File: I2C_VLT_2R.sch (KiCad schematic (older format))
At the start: 5 parts, among them Q14 BSS138, Q15 BSS138

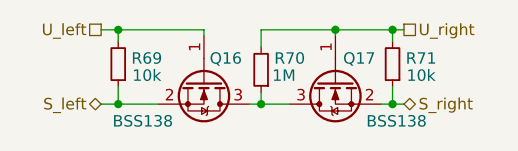
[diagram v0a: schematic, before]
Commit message: Завершена трассировка печатной платы. Исправлены ошибки в схема.
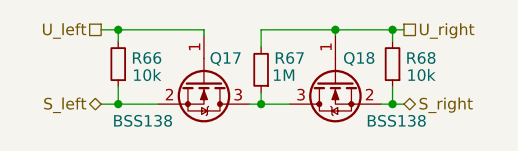
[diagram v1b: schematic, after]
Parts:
- renumbered Q14 to Q17, Q15 to Q18
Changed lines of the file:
@@
 AR Path="/63EB474D/6022B564" Ref="Q?"  Part="1"
 AR Path="/64080380/6022B564" Ref="Q?"  Part="1"
-AR Path="/61C817F1/61DF5D35/6022B564" Ref="Q14"  Part="1"
-AR Path="/61C817F1/61DF5D57/6022B564" Ref="Q16"  Part="1"
+AR Path="/61C817F1/61DF5D35/6022B564" Ref="Q17"  Part="1"
+AR Path="/61C817F1/61DF5D57/6022B564" Ref="Q19"  Part="1"
 AR Path="/63E242A3/61DF5D35/6022B564" Ref="Q?"  Part="1"
 AR Path="/63E242A3/61DF5D57/6022B564" Ref="Q?"  Part="1"
-F 0 "Q16" V 5225 1800 50  0000 L CNN
+F 0 "Q17" V 5225 1800 50  0000 L CNN
 F 1 "BSS138" V 5500 1375 50  0000 L CNN
 F 2 "Package_TO_SOT_SMD:SOT-23" H 5525 1700 50  0001 L CIN
@@
 AR Path="/63E242A3/61DF5D35/6022B56A" Ref="R?"  Part="1"
 AR Path="/63E242A3/61DF5D57/6022B56A" Ref="R?"  Part="1"
-F 0 "R70" H 5450 1675 50  0000 C CNN
+F 0 "R67" H 5450 1675 50  0000 C CNN
 F 1 "1M" H 5475 1750 50  0000 C CNN
 F 2 "Resistor_SMD:R_0603_1608Metric" H 5575 1725 50  0001 C CNN
@@
 AR Path="/63EB474D/6022B576" Ref="Q?"  Part="1"
 AR Path="/64080380/6022B576" Ref="Q?"  Part="1"
-AR Path="/61C817F1/61DF5D35/6022B576" Ref="Q15"  Part="1"
-AR Path="/61C817F1/61DF5D57/6022B576" Ref="Q17"  Part="1"
+AR Path="/61C817F1/61DF5D35/6022B576" Ref="Q18"  Part="1"
+AR Path="/61C817F1/61DF5D57/6022B576" Ref="Q20"  Part="1"
 AR Path="/63E242A3/61DF5D35/6022B576" Ref="Q?"  Part="1"
 AR Path="/63E242A3/61DF5D57/6022B576" Ref="Q?"  Part="1"
-F 0 "Q17" V 5800 1600 50  0000 L CNN
+F 0 "Q18" V 5800 1600 50  0000 L CNN
 F 1 "BSS138" V 6075 1375 50  0000 L CNN
 F 2 "Package_TO_SOT_SMD:SOT-23" H 6100 1700 50  0001 L CIN
@@
 AR Path="/63E242A3/61DF5D35/6654E38D" Ref="R?"  Part="1"
 AR Path="/63E242A3/61DF5D57/6654E38D" Ref="R?"  Part="1"
-F 0 "R69" H 4825 1675 50  0000 C CNN
+F 0 "R66" H 4825 1675 50  0000 C CNN
 F 1 "10k" H 4825 1750 50  0000 C CNN
 F 2 "Resistor_SMD:R_0603_1608Metric" H 4950 1700 50  0001 C CNN
@@
 AR Path="/63E242A3/61DF5D35/6654F436" Ref="R?"  Part="1"
 AR Path="/63E242A3/61DF5D57/6654F436" Ref="R?"  Part="1"
-F 0 "R71" H 6025 1675 50  0000 C CNN
+F 0 "R68" H 6025 1675 50  0000 C CNN
 F 1 "10k" H 6025 1750 50  0000 C CNN
 F 2 "Resistor_SMD:R_0603_1608Metric" H 6150 1700 50  0001 C CNN

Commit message: Сформирован перечень элементов, 3D-модель, исправлены ошибки, реализована панелизация платы.
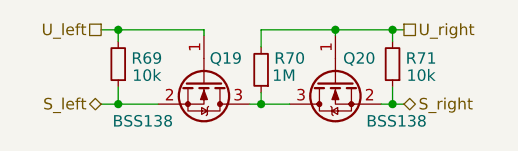
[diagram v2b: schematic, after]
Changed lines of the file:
@@
 AR Path="/63E242A3/61DF5D35/6022B564" Ref="Q?"  Part="1"
 AR Path="/63E242A3/61DF5D57/6022B564" Ref="Q?"  Part="1"
-F 0 "Q17" V 5225 1800 50  0000 L CNN
+F 0 "Q19" V 5225 1800 50  0000 L CNN
 F 1 "BSS138" V 5500 1375 50  0000 L CNN
 F 2 "Package_TO_SOT_SMD:SOT-23" H 5525 1700 50  0001 L CIN
@@
 AR Path="/63E242A3/61DF5D35/6022B56A" Ref="R?"  Part="1"
 AR Path="/63E242A3/61DF5D57/6022B56A" Ref="R?"  Part="1"
-F 0 "R67" H 5450 1675 50  0000 C CNN
+F 0 "R70" H 5450 1675 50  0000 C CNN
 F 1 "1M" H 5475 1750 50  0000 C CNN
 F 2 "Resistor_SMD:R_0603_1608Metric" H 5575 1725 50  0001 C CNN
@@
 AR Path="/63E242A3/61DF5D35/6022B576" Ref="Q?"  Part="1"
 AR Path="/63E242A3/61DF5D57/6022B576" Ref="Q?"  Part="1"
-F 0 "Q18" V 5800 1600 50  0000 L CNN
+F 0 "Q20" V 5800 1600 50  0000 L CNN
 F 1 "BSS138" V 6075 1375 50  0000 L CNN
 F 2 "Package_TO_SOT_SMD:SOT-23" H 6100 1700 50  0001 L CIN
@@
 AR Path="/63E242A3/61DF5D35/6654E38D" Ref="R?"  Part="1"
 AR Path="/63E242A3/61DF5D57/6654E38D" Ref="R?"  Part="1"
-F 0 "R66" H 4825 1675 50  0000 C CNN
+F 0 "R69" H 4825 1675 50  0000 C CNN
 F 1 "10k" H 4825 1750 50  0000 C CNN
 F 2 "Resistor_SMD:R_0603_1608Metric" H 4950 1700 50  0001 C CNN
@@
 AR Path="/63E242A3/61DF5D35/6654F436" Ref="R?"  Part="1"
 AR Path="/63E242A3/61DF5D57/6654F436" Ref="R?"  Part="1"
-F 0 "R68" H 6025 1675 50  0000 C CNN
+F 0 "R71" H 6025 1675 50  0000 C CNN
 F 1 "10k" H 6025 1750 50  0000 C CNN
 F 2 "Resistor_SMD:R_0603_1608Metric" H 6150 1700 50  0001 C CNN
